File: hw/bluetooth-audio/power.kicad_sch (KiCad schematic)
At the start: 46 parts, among them J2 USB_C_Receptacle_USB2.0, J5 Conn_01x03, U11 LP5907MFX-3.3, U5 USBLC6-2SC6, U7 AP7361C-33Y5, U9 BQ24074RGT

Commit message: BOM: move C51, charger resistors and D1 to JLCPCB Basic parts
Cuts Extended (paid-setup) parts from 25 to 20 without changing any circuit
values:
- C51 USB-shield filter 4.7nF: 1206 -> 0402, Basic C1538 (generic filter cap).
- R_TMR1/R_ISET1/R_ITERM1 (56k/1.2k/3k charger programming): 0402 -> 0603 to
  get Basic parts at the SAME values (C23206/C22765/C4211) - charger behaviour
  unchanged; no Basic exists at these values in 0402.
- D1: no blue LED is a JLCPCB Basic part, so changed to white (C34499, Basic);
  value relabelled LED_WHITE. GPIO net still named LED_BLUE.

Left Extended (no Basic option / intentional):
- C37/C38 are the 2.4GHz antenna-match caps (need NP0), not crystal-load caps;
  no Basic 3.3pF exists. Crystal-load caps are C35/C36 (already Basic C0G).
- Q1 UMH3N: no Basic dual/single digital transistor - see docs/bom-audit.md
  section 6 (keep Extended vs redesign to 2x MMBT3904 + resistors).

docs/bom-audit.md updated with the changes and revised cost (~$11.24/board @30).

Co-Authored-By: Claude Opus 4.8 <noreply@anthropic.com>
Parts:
- C51: footprint Capacitor_SMD:C_1206_3216Metric -> Capacitor_SMD:C_0402_1005Metric; LCSC C113886 -> C1538; MPN CC1206JRNPO9BN472 -> 0402B472K500NT; Manufacturer YAGEO -> FH Guangdong Fenghua Advanced Tech
- R_ISET1: footprint Resistor_SMD:R_0402_1005Metric -> Resistor_SMD:R_0603_1608Metric; LCSC C2909307 -> C22765; MPN FRC0402F1201TS -> 0603WAF1201T5E; Manufacturer FOJAN -> UNI ROYAL Uniroyal Elec
- R_ITERM1: footprint Resistor_SMD:R_0402_1005Metric -> Resistor_SMD:R_0603_1608Metric; LCSC C2909355 -> C4211; MPN FRC0402F3001TS -> 0603WAF3001T5E; Manufacturer FOJAN -> UNI ROYAL Uniroyal Elec
- R_TMR1: footprint Resistor_SMD:R_0402_1005Metric -> Resistor_SMD:R_0603_1608Metric; LCSC C2906875 -> C23206; MPN FRC0402F5602TS -> 0603WAF5602T5E; Manufacturer FOJAN -> UNI ROYAL Uniroyal Elec
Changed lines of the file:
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@@
 			)
 		)
-		(property "Footprint" "Resistor_SMD:R_0402_1005Metric"
+		(property "Footprint" "Resistor_SMD:R_0603_1608Metric"
 			(at 96.52 138.938 90)
 			(hide yes)
@@
 			)
 		)
-		(property "Manufacturer" "FOJAN"
+		(property "Manufacturer" "UNI ROYAL Uniroyal Elec"
 			(at 96.52 137.16 0)
 			(hide yes)
@@
 			)
 		)
-		(property "MPN" "FRC0402F5602TS"
+		(property "MPN" "0603WAF5602T5E"
 			(at 96.52 137.16 0)
 			(hide yes)
@@
 			)
 		)
-		(property "LCSC" "C2906875"
+		(property "LCSC" "C23206"
 			(at 96.52 137.16 0)
 			(hide yes)
@@
 			)
 		)
-		(property "Footprint" "Capacitor_SMD:C_1206_3216Metric"
+		(property "Footprint" "Capacitor_SMD:C_0402_1005Metric"
 			(at 29.21 86.36 0)
 			(hide yes)
@@
 			)
 		)
-		(property "Manufacturer" "YAGEO"
+		(property "Manufacturer" "FH Guangdong Fenghua Advanced Tech"
 			(at 29.21 86.36 0)
 			(hide yes)
@@
 			)
 		)
-		(property "MPN" "CC1206JRNPO9BN472"
+		(property "MPN" "0402B472K500NT"
 			(at 29.21 86.36 0)
 			(hide yes)
@@
 			)
 		)
-		(property "LCSC" "C113886"
+		(property "LCSC" "C1538"
 			(at 29.21 86.36 0)
 			(hide yes)
@@
 			)
 		)
-		(property "Footprint" "Resistor_SMD:R_0402_1005Metric"
+		(property "Footprint" "Resistor_SMD:R_0603_1608Metric"
 			(at 96.52 124.968 90)
 			(hide yes)
@@
 			)
 		)
-		(property "Manufacturer" "FOJAN"
+		(property "Manufacturer" "UNI ROYAL Uniroyal Elec"
 			(at 96.52 123.19 0)
 			(hide yes)
@@
 			)
 		)
-		(property "MPN" "FRC0402F3001TS"
+		(property "MPN" "0603WAF3001T5E"
 			(at 96.52 123.19 0)
 			(hide yes)
@@
 			)
 		)
-		(property "LCSC" "C2909355"
+		(property "LCSC" "C4211"
 			(at 96.52 123.19 0)
 			(hide yes)
@@
 			)
 		)
-		(property "Footprint" "Resistor_SMD:R_0402_1005Metric"
+		(property "Footprint" "Resistor_SMD:R_0603_1608Metric"
 			(at 105.918 168.91 90)
 			(hide yes)
@@
 			)
 		)
-		(property "Manufacturer" "FOJAN"
+		(property "Manufacturer" "UNI ROYAL Uniroyal Elec"
 			(at 104.14 168.91 0)
 			(hide yes)
@@
 			)
 		)
-		(property "MPN" "FRC0402F1201TS"
+		(property "MPN" "0603WAF1201T5E"
 			(at 104.14 168.91 0)
 			(hide yes)
@@
 			)
 		)
-		(property "LCSC" "C2909307"
+		(property "LCSC" "C22765"
 			(at 104.14 168.91 0)
 			(hide yes)

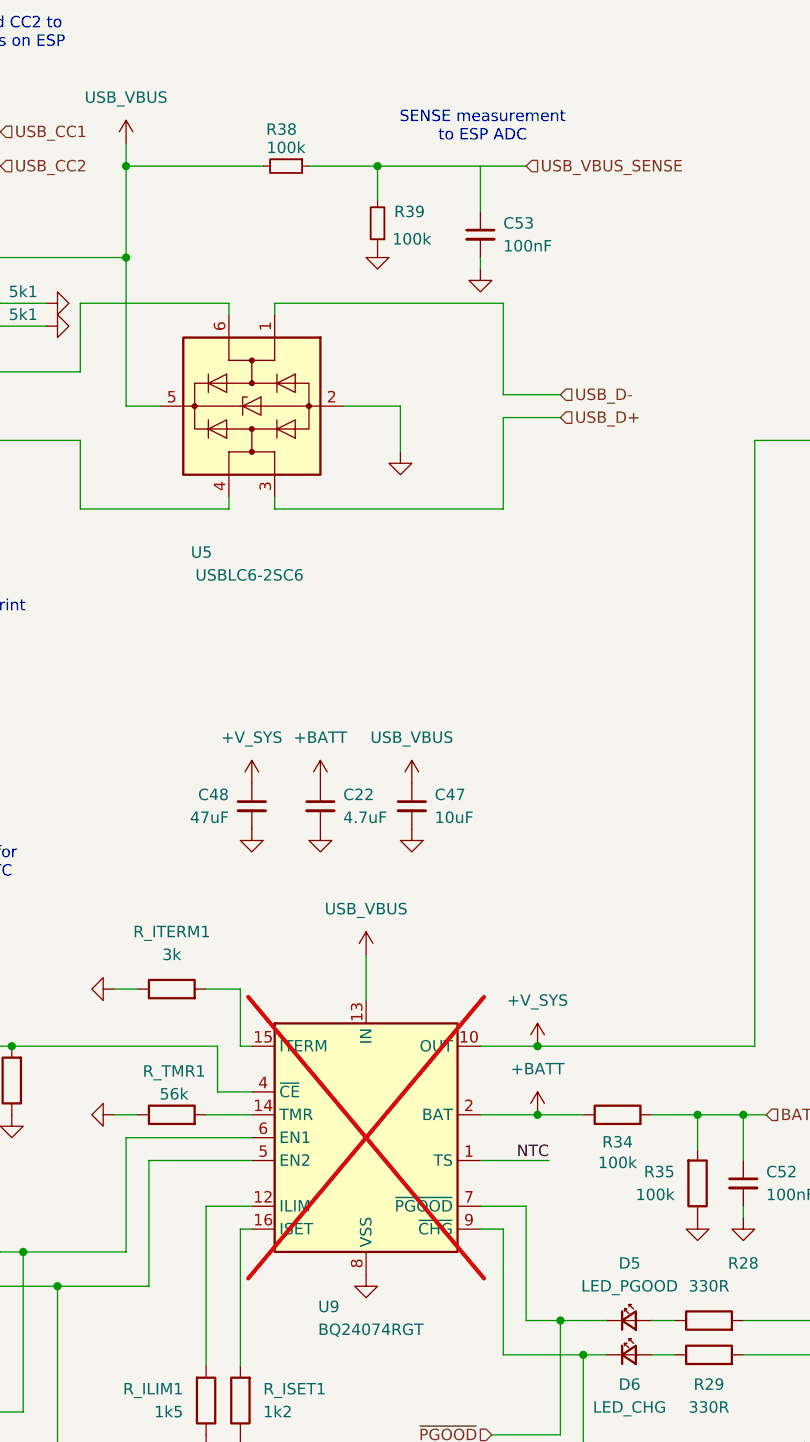
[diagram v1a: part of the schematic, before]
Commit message: Audio BOM: OUT2 couplers to electrolytic, C53 0402, C41/C42 land; place PCB
Schematic (audio + power sheets):
- C24/C26 (ES8388 OUT2 -> TP6 test-output couplers): 1uF MLCC -> 47uF
  electrolytic (Panasonic EEEFT1E470AR / C336270), matching C1/C21. Polarity
  verified against the netlist: + terminal to the codec/VMID side.
- C53 (USB_VBUS_SENSE divider filter): 1206 -> 0402 (house part
  CL05B104KO5NNNC / C1525).
- C41/C42 (mic C0G couplers): footprint aligned to plain C_1206_3216Metric,
  matching C54.

PCB: all footprints now placed in their initial positions, pending V1 routing.

Docs: design-overview.tex updated (delta #20 + 2026-09-16 revision entry). The
D7/D8 TX-input clamp removal is decided but recorded as pending -- that
schematic edit is being done by hand and is not in this commit.

Note: the deleted kicad-library submodule and the untracked in-project library
copies are deliberately left unstaged (broken/redundant state).

Co-Authored-By: Claude Opus 4.8 <noreply@anthropic.com>
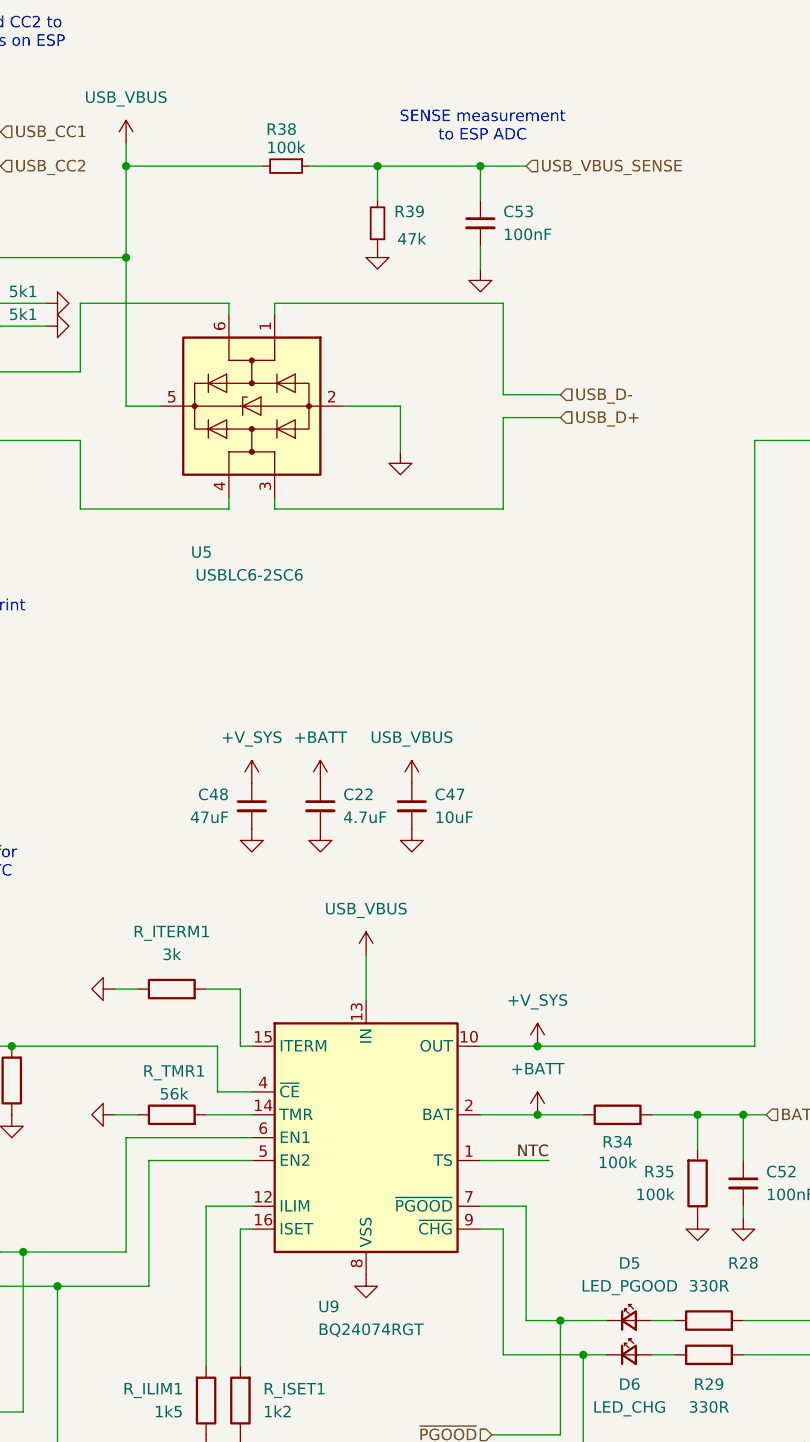
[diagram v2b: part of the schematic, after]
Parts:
- C53: footprint Capacitor_SMD:C_1206_3216Metric -> Capacitor_SMD:C_0402_1005Metric; LCSC C24497 -> C1525; MPN CL31B104KBCNNNC -> CL05B104KO5NNNC
- R39: value 100k -> 47k; LCSC C25741 -> C25792; MPN 0402WGF1003TCE -> 0402WGF4702TCE
- R_ISET1: footprint Resistor_SMD:R_0603_1608Metric -> Resistor_SMD:R_0402_1005Metric; LCSC C22765 -> C25862; MPN 0603WAF1201T5E -> 0402WGF1201TCE
- R_ITERM1: footprint Resistor_SMD:R_0603_1608Metric -> Resistor_SMD:R_0402_1005Metric; LCSC C4211 -> C25784; MPN 0603WAF3001T5E -> 0402WGF3001TCE
- R_TMR1: footprint Resistor_SMD:R_0603_1608Metric -> Resistor_SMD:R_0402_1005Metric; LCSC C23206 -> C25796; MPN 0603WAF5602T5E -> 0402WGF5602TCE
- U9: now fitted
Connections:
- net USB_VBUS_SENSE: now also C53.1
